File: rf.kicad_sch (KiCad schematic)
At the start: 13 parts, among them J12 ${MANUFACTURER PART NUMBER}, Q6 ${MANUFACTURER PART NUMBER}, U10 ${MANUFACTURER PART NUMBER}, U11 ${MANUFACTURER PART NUMBER}, U12 ${MANUFACTURER PART NUMBER}, U9 ${MANUFACTURER PART NUMBER}

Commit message: Add initial layout for the GNSS receiver
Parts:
- L3: footprint (none) -> passive_inductor:L_0402_Density_Nominal
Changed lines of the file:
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@@
 			)
 		)
-		(property "Footprint" ""
+		(property "Footprint" "passive_inductor:L_0402_Density_Nominal"
 			(at 100.33 39.37 0)
 			(hide yes)

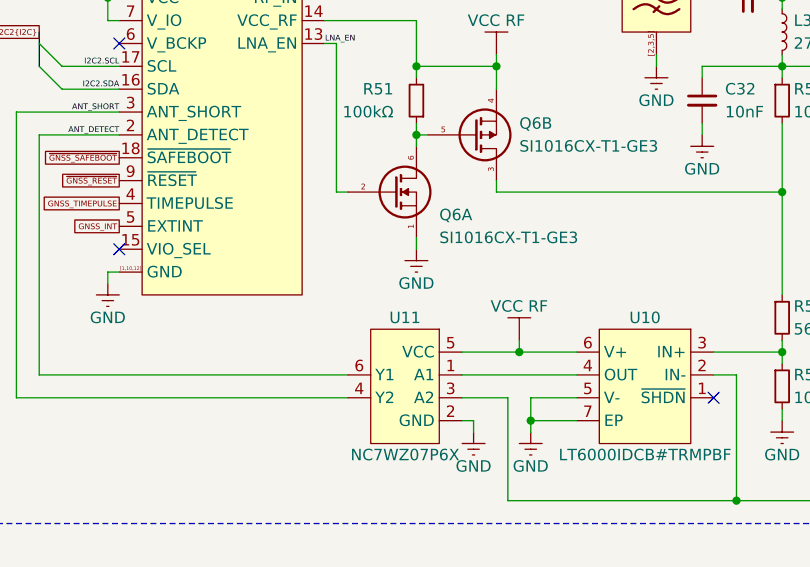
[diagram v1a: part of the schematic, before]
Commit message: Improve board grounding for RF
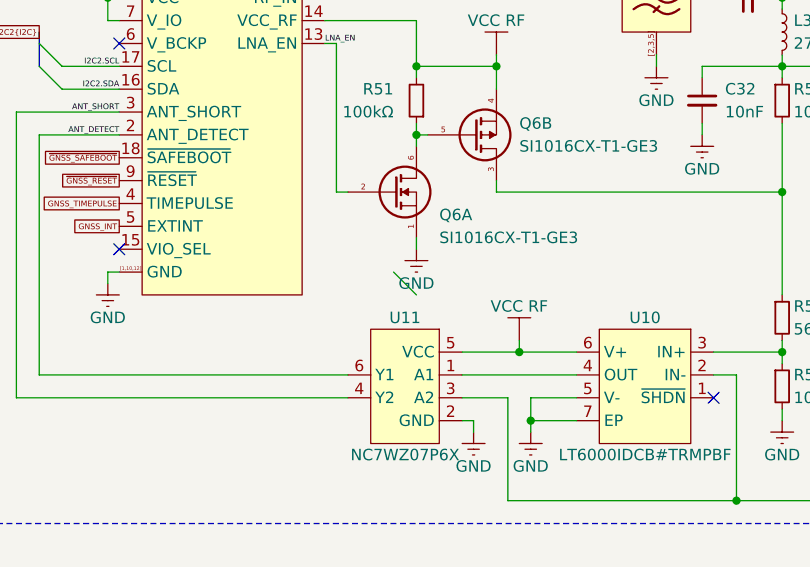
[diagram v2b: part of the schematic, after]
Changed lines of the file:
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@@
+	)
+	(bus_entry
+		(at 57.15 54.61)
+		(size 2.54 2.54)
+		(stroke
+			(width 0)
+			(type default)
+		)
 	)
 	(bus_entry
@@
 		(in_pos_files yes)
 		(dnp no)
-		(fields_autoplaced yes)
 		(property "Reference" "#PWR062"
 			(at 59.69 62.23 0)

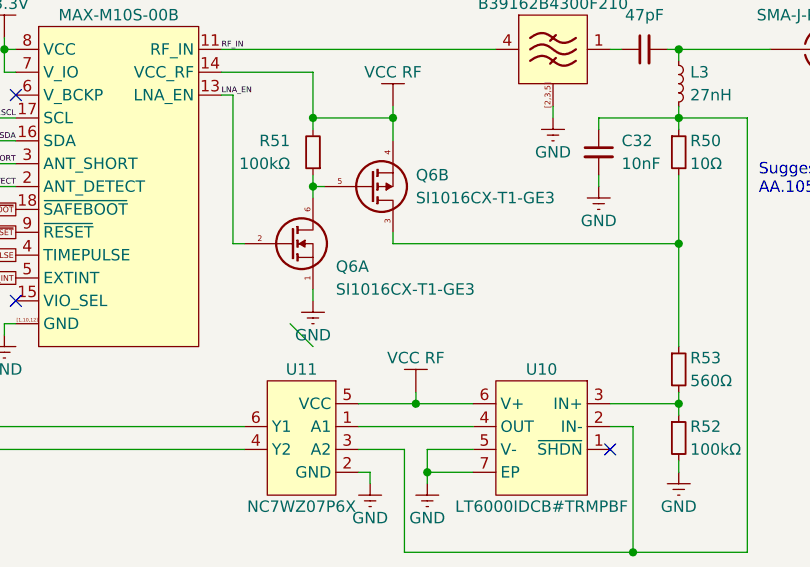
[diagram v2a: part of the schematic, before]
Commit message: Major fix: move from a flat to a hierarchical architecture for schematic.
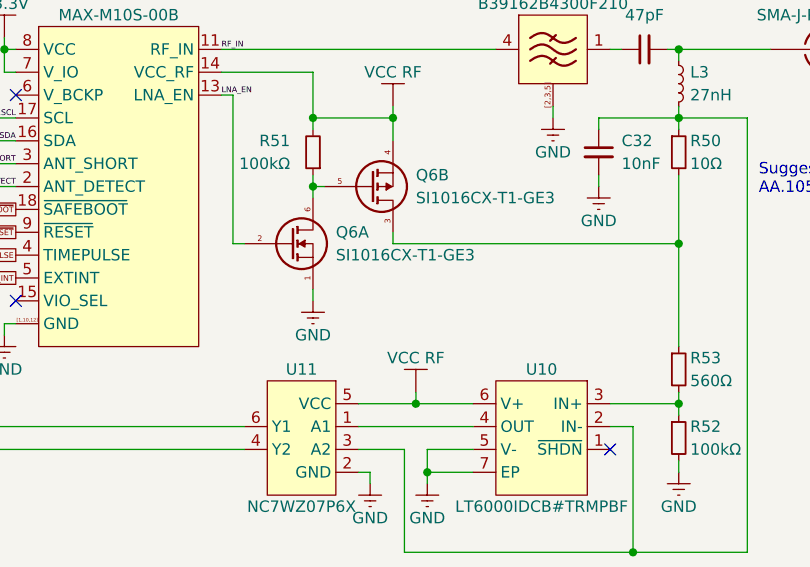
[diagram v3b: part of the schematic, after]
